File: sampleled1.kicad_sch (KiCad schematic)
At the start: 2 parts

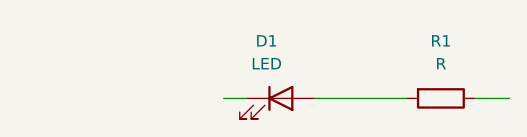
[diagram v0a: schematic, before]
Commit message: push button added
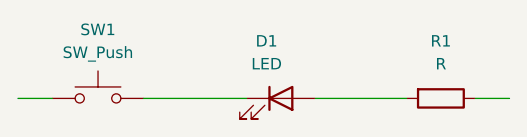
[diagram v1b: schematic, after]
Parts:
- added SW1: SW_Push, symbol Switch:SW_Push
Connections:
- net at D1.1 (K): now also SW1.2
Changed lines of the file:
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@@
+	(wire
+		(pts
+			(xy 100.33 64.77) (xy 111.76 64.77)
+		)
+		(stroke
+			(width 0)
+			(type default)
+		)
+	)
+	(wire
+		(pts
+			(xy 86.36 64.77) (xy 90.17 64.77)
+		)
+		(stroke
+			(width 0)
+			(type default)
+		)
+	)
 	(wire
 		(pts
@@
 		)
 	)
-	(wire
-		(pts
-			(xy 109.22 64.77) (xy 111.76 64.77)
+	(symbol
+		(lib_id "Switch:SW_Push")
+		(at 95.25 64.77 0)
+		(unit 1)
+		(exclude_from_sim no)
+		(in_bom yes)
+		(on_board yes)
+		(dnp no)
+		(fields_autoplaced yes)
+		(property "Reference" "SW1"
+			(at 95.25 57.15 0)
+			(effects
+				(font
+					(size 1.27 1.27)
+				)
+			)
 		)
-		(stroke
-			(width 0)
-			(type default)
+		(property "Value" "SW_Push"
+			(at 95.25 59.69 0)
+			(effects
+				(font
+					(size 1.27 1.27)
+				)
+			)
+		)
+		(property "Footprint" ""
+			(at 95.25 59.69 0)
+			(effects
+				(font
+					(size 1.27 1.27)
+				)
+				(hide yes)
+			)
+		)
+		(property "Datasheet" "~"
+			(at 95.25 59.69 0)
+			(effects
+				(font
+					(size 1.27 1.27)
+				)
+				(hide yes)
+			)
+		)
+		(property "Description" "Push button switch, generic, two pins"
+			(at 95.25 64.77 0)
+			(effects
+				(font
+					(size 1.27 1.27)
+				)
+				(hide yes)
+			)
+		)
+		(pin "2"
+		)
+		(pin "1"
+		)
+		(instances
+			(project ""
+				(path "/32f4ff92-77d1-4923-bce0-aa147d562103"
+					(reference "SW1")
+					(unit 1)
+				)
+			)
 		)
 	)

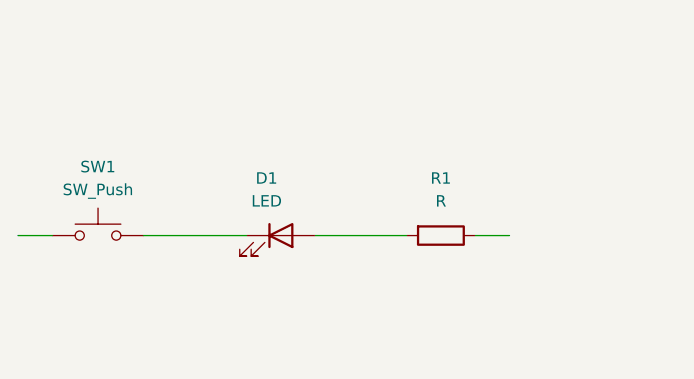
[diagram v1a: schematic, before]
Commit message: battery added
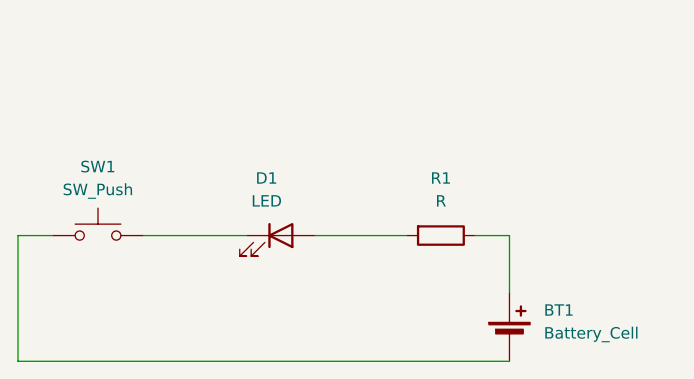
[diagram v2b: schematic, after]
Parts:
- added BT1: Battery_Cell, symbol Device:Battery_Cell
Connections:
- net at SW1.1: now also BT1.2 (-)
- net at R1.1: now also BT1.1 (+)
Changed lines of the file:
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@@
+	(wire
+		(pts
+			(xy 86.36 78.74) (xy 140.97 78.74)
+		)
+		(stroke
+			(width 0)
+			(type default)
+		)
+	)
 	(wire
 		(pts
@@
 		(pts
 			(xy 86.36 64.77) (xy 90.17 64.77)
+		)
+		(stroke
+			(width 0)
+			(type default)
+		)
+	)
+	(wire
+		(pts
+			(xy 140.97 64.77) (xy 140.97 71.12)
+		)
+		(stroke
+			(width 0)
+			(type default)
+		)
+	)
+	(wire
+		(pts
+			(xy 86.36 64.77) (xy 86.36 78.74)
 		)
 		(stroke
@@
 					(unit 1)
 				)
+			)
+		)
+	)
+	(symbol
+		(lib_id "Device:Battery_Cell")
+		(at 140.97 76.2 0)
+		(unit 1)
+		(exclude_from_sim no)
+		(in_bom yes)
+		(on_board yes)
+		(dnp no)
+		(fields_autoplaced yes)
+		(property "Reference" "BT1"
+			(at 144.78 73.0884 0)
+			(effects
+				(font
+					(size 1.27 1.27)
+				)
+				(justify left)
+			)
+		)
+		(property "Value" "Battery_Cell"
+			(at 144.78 75.6284 0)
+			(effects
+				(font
+					(size 1.27 1.27)
+				)
+				(justify left)
+			)
+		)
+		(property "Footprint" ""
+			(at 140.97 74.676 90)
+			(effects
+				(font
+					(size 1.27 1.27)
+				)
+				(hide yes)
+			)
+		)
+		(property "Datasheet" "~"
+			(at 140.97 74.676 90)
+			(effects
+				(font
+					(size 1.27 1.27)
+				)
+				(hide yes)
+			)
+		)
+		(property "Description" "Single-cell battery"
+			(at 140.97 76.2 0)
+			(effects
+				(font
+					(size 1.27 1.27)
+				)
+				(hide yes)
+			)
+		)
+		(pin "1"
+		)
+		(pin "2"
+		)
+		(instances
+			(project ""
+				(path "/32f4ff92-77d1-4923-bce0-aa147d562103"
+					(reference "BT1")
+					(unit 1)
+				)

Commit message: led2 added
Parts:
- added D2: LED, symbol Device:LED
- added R2: R, symbol Device:R
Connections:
- net at D1.1 (K), SW1.2: now also D2.1 (K)
- net at BT1.1 (+), R1.1: now also R2.1
- new net: D2.2 (A), R2.2
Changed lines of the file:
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@@
 	(generator_version "8.0")
 	(paper "A4")
+	(junction
+		(at 111.76 64.77)
+		(diameter 0)
+		(color 0 0 0 0)
+	)
+	(junction
+		(at 137.16 64.77)
+		(diameter 0)
+		(color 0 0 0 0)
+	)
 	(wire
 		(pts
@@
 	(wire
 		(pts
+			(xy 119.38 50.8) (xy 129.54 50.8)
+		)
+		(stroke
+			(width 0)
+			(type default)
+		)
+	)
+	(wire
+		(pts
 			(xy 140.97 64.77) (xy 140.97 71.12)
 		)
@@
 	(wire
 		(pts
+			(xy 111.76 50.8) (xy 111.76 64.77)
+		)
+		(stroke
+			(width 0)
+			(type default)
+		)
+	)
+	(wire
+		(pts
 			(xy 86.36 64.77) (xy 86.36 78.74)
 		)
@@
 		(pts
 			(xy 137.16 64.77) (xy 140.97 64.77)
+		)
+		(stroke
+			(width 0)
+			(type default)
+		)
+	)
+	(wire
+		(pts
+			(xy 137.16 50.8) (xy 137.16 64.77)
 		)
 		(stroke
@@
 	(symbol
 		(lib_id "Device:R")
+		(at 133.35 50.8 270)
+		(unit 1)
+		(exclude_from_sim no)
+		(in_bom yes)
+		(on_board yes)
+		(dnp no)
+		(fields_autoplaced yes)
+		(property "Reference" "R2"
+			(at 133.35 44.45 90)
+			(effects
+				(font
+					(size 1.27 1.27)
+				)
+			)
+		)
+		(property "Value" "R"
+			(at 133.35 46.99 90)
+			(effects
+				(font
+					(size 1.27 1.27)
+				)
+			)
+		)
+		(property "Footprint" ""
+			(at 133.35 49.022 90)
+			(effects
+				(font
+					(size 1.27 1.27)
+				)
+				(hide yes)
+			)
+		)
+		(property "Datasheet" "~"
+			(at 133.35 50.8 0)
+			(effects
+				(font
+					(size 1.27 1.27)
+				)
+				(hide yes)
+			)
+		)
+		(property "Description" "Resistor"
+			(at 133.35 50.8 0)
+			(effects
+				(font
+					(size 1.27 1.27)
+				)
+				(hide yes)
+			)
+		)
+		(pin "1"
+		)
+		(pin "2"
+		)
+		(instances
+			(project "sampleled1"
+				(path "/32f4ff92-77d1-4923-bce0-aa147d562103"
+					(reference "R2")
+					(unit 1)
+				)
+			)
+		)
+	)
+	(symbol
+		(lib_id "Device:R")
 		(at 133.35 64.77 270)
 		(unit 1)
@@
 					(unit 1)
 				)
+			)
+		)
+	)
+	(symbol
+		(lib_id "Device:LED")
+		(at 115.57 50.8 0)
+		(unit 1)
+		(exclude_from_sim no)
+		(in_bom yes)
+		(on_board yes)
+		(dnp no)
+		(fields_autoplaced yes)
+		(property "Reference" "D2"
+			(at 113.9825 44.45 0)
+			(effects
+				(font
+					(size 1.27 1.27)
+				)
+			)
+		)
+		(property "Value" "LED"
+			(at 113.9825 46.99 0)
+			(effects
+				(font
+					(size 1.27 1.27)
+				)
+			)
+		)
+		(property "Footprint" ""
+			(at 115.57 50.8 0)
+			(effects
+				(font
+					(size 1.27 1.27)
+				)
+				(hide yes)
+			)
+		)
+		(property "Datasheet" "~"
+			(at 115.57 50.8 0)
+			(effects
+				(font
+					(size 1.27 1.27)
+				)
+				(hide yes)
+			)
+		)
+		(property "Description" "Light emitting diode"
+			(at 115.57 50.8 0)
+			(effects
+				(font
+					(size 1.27 1.27)
+				)
+				(hide yes)
+			)
+		)
+		(pin "2"
+		)
+		(pin "1"
+		)
+		(instances
+			(project "sampleled1"
+				(path "/32f4ff92-77d1-4923-bce0-aa147d562103"
+					(reference "D2")
+					(unit 1)
+				)

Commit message: schmeatic added
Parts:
- added SW2: SW_Push, symbol Switch:SW_Push
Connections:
- net at BT1.2 (-), SW1.1: now also SW2.1
- net at D1.1 (K), D2.1 (K), SW1.2: now also SW2.2
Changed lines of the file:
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@@
 	(paper "A4")
 	(junction
+		(at 90.17 64.77)
+		(diameter 0)
+		(color 0 0 0 0)
+	)
+	(junction
 		(at 111.76 64.77)
 		(diameter 0)
@@
 		(color 0 0 0 0)
 	)
+	(junction
+		(at 100.33 64.77)
+		(diameter 0)
+		(color 0 0 0 0)
+	)
 	(wire
 		(pts
@@
 	(wire
 		(pts
+			(xy 100.33 49.53) (xy 100.33 64.77)
+		)
+		(stroke
+			(width 0)
+			(type default)
+		)
+	)
+	(wire
+		(pts
 			(xy 86.36 64.77) (xy 90.17 64.77)
 		)
@@
 		(pts
 			(xy 119.38 50.8) (xy 129.54 50.8)
+		)
+		(stroke
+			(width 0)
+			(type default)
+		)
+	)
+	(wire
+		(pts
+			(xy 90.17 49.53) (xy 90.17 64.77)
 		)
 		(stroke
@@
 					(unit 1)
 				)
+			)
+		)
+	)
+	(symbol
+		(lib_id "Switch:SW_Push")
+		(at 95.25 49.53 0)
+		(unit 1)
+		(exclude_from_sim no)
+		(in_bom yes)
+		(on_board yes)
+		(dnp no)
+		(fields_autoplaced yes)
+		(property "Reference" "SW2"
+			(at 95.25 41.91 0)
+			(effects
+				(font
+					(size 1.27 1.27)
+				)
+			)
+		)
+		(property "Value" "SW_Push"
+			(at 95.25 44.45 0)
+			(effects
+				(font
+					(size 1.27 1.27)
+				)
+			)
+		)
+		(property "Footprint" ""
+			(at 95.25 44.45 0)
+			(effects
+				(font
+					(size 1.27 1.27)
+				)
+				(hide yes)
+			)
+		)
+		(property "Datasheet" "~"
+			(at 95.25 44.45 0)
+			(effects
+				(font
+					(size 1.27 1.27)
+				)
+				(hide yes)
+			)
+		)
+		(property "Description" "Push button switch, generic, two pins"
+			(at 95.25 49.53 0)
+			(effects
+				(font
+					(size 1.27 1.27)
+				)
+				(hide yes)
+			)
+		)
+		(pin "2"
+		)
+		(pin "1"
+		)
+		(instances
+			(project "sampleled1"
+				(path "/32f4ff92-77d1-4923-bce0-aa147d562103"
+					(reference "SW2")
+					(unit 1)
+				)

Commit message: THT Footprint assigned
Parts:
- BT1: footprint (none) -> Battery:BatteryHolder_Bulgin_BX0036_1xC
- D1, D2: footprint (none) -> LED_THT:LED_D5.0mm_IRGrey
- R1, R2: footprint (none) -> Resistor_THT:R_Axial_DIN0204_L3.6mm_D1.6mm_P1.90mm_Vertical
- SW1, SW2: footprint (none) -> Button_Switch_THT:SW_PUSH_6mm
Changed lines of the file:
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@@
 			)
 		)
-		(property "Footprint" ""
+		(property "Footprint" "Button_Switch_THT:SW_PUSH_6mm"
 			(at 95.25 59.69 0)
 			(effects
@@
 			)
 		)
-		(property "Footprint" ""
+		(property "Footprint" "Button_Switch_THT:SW_PUSH_6mm"
 			(at 95.25 44.45 0)
 			(effects
@@
 			)
 		)
-		(property "Footprint" ""
+		(property "Footprint" "Resistor_THT:R_Axial_DIN0204_L3.6mm_D1.6mm_P1.90mm_Vertical"
 			(at 133.35 49.022 90)
 			(effects
@@
 			)
 		)
-		(property "Footprint" ""
+		(property "Footprint" "Resistor_THT:R_Axial_DIN0204_L3.6mm_D1.6mm_P1.90mm_Vertical"
 			(at 133.35 62.992 90)
 			(effects
@@
 			)
 		)
-		(property "Footprint" ""
+		(property "Footprint" "Battery:BatteryHolder_Bulgin_BX0036_1xC"
 			(at 140.97 74.676 90)
 			(effects
@@
 			)
 		)
-		(property "Footprint" ""
+		(property "Footprint" "LED_THT:LED_D5.0mm_IRGrey"
 			(at 115.57 50.8 0)
 			(effects
@@
 			)
 		)
-		(property "Footprint" ""
+		(property "Footprint" "LED_THT:LED_D5.0mm_IRGrey"
 			(at 115.57 64.77 0)
 			(effects
